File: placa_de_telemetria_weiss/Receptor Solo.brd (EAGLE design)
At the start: 61.9 x 84.3 mm, 6 parts

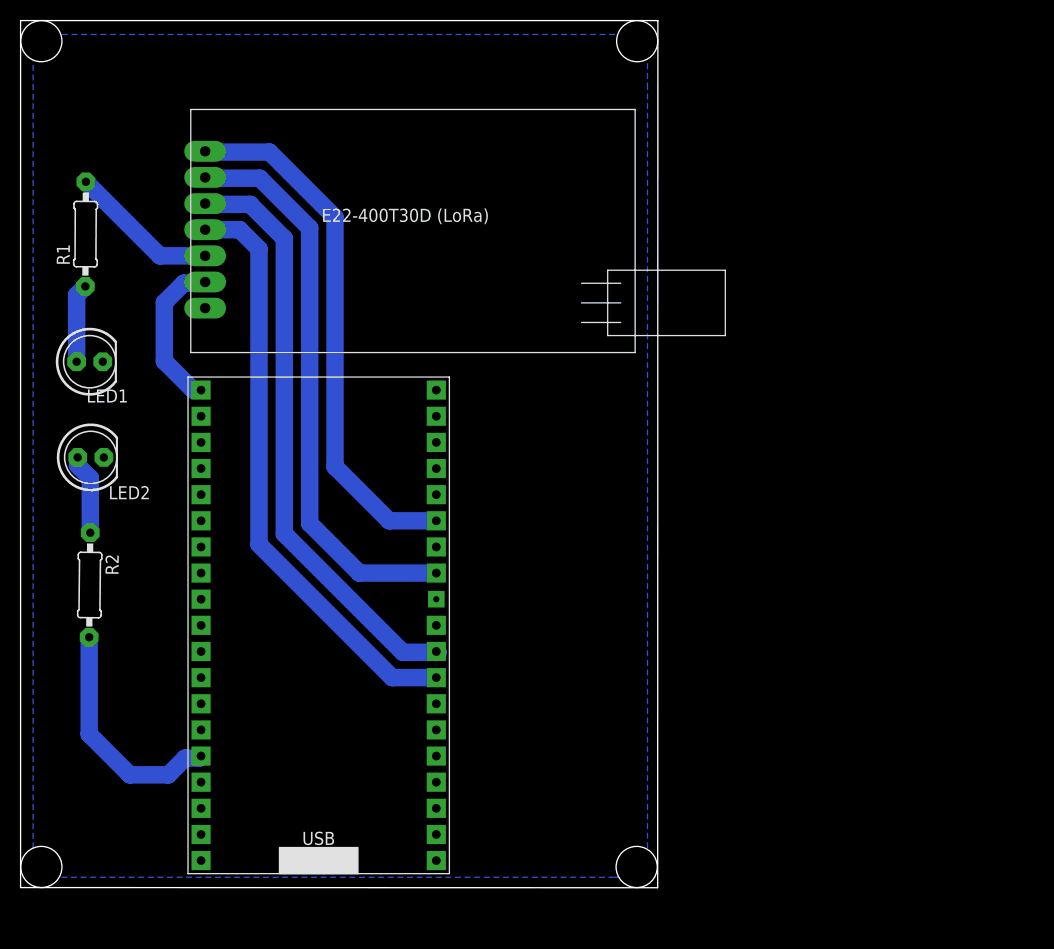
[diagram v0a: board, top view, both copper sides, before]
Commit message: fix(pcb): substitui ESP32 incorreto e adiciona furos de fixação à placa de telemetria
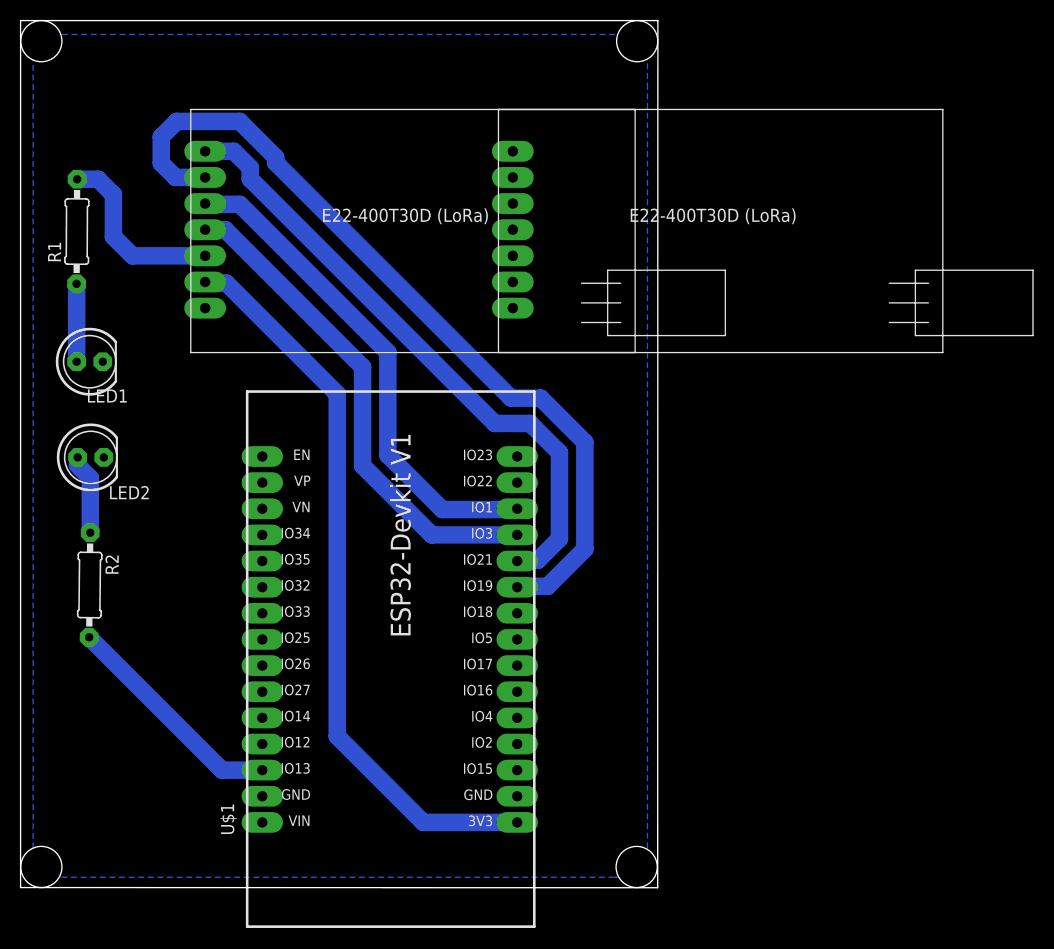
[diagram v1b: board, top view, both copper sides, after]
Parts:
- added FUROSDEAPOIOLORA: E22-400T30D, CRD:E22-400T30D_FOOTPRINT
- U$1: value ESP32 -> ESP32DEVKITV1; device esp32:ESP32 -> ESP32-DEVKITV1:ESP32-DEVKITV1
- moved U$1 33.4 mm to (49.0, 26.6), turned to 90 degrees
- moved R1 0.89 mm to (19.7, 61.1)
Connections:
- net N$6 renamed AUX
- removed net N$1: U$1.GPIO21, U$2.M0
- removed net N$2: U$1.GPIO19, U$2.M1
- removed net N$3: U$1.GPIO17, U$2.RXD
- removed net N$4: U$1.GPIO16, U$2.TXD
- removed net N$5: R2.2, U$1.GPIO13
- removed net VCC: U$1.3.3V, U$2.VCC
- new net 3.3V: U$1.1, U$2.VCC
- new net GPIO13: R2.2, U$1.28
- new net GPIO19: U$1.10, U$2.M1
- new net GPIO21: U$1.11, U$2.M0
- new net RXLORA: U$1.13, U$2.RXD
- new net TXLORA: U$1.12, U$2.TXD
- net GND: now also U$1.2, U$1.29; no longer U$1.GND1
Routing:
- net GPIO19: track 0.00 -> 80.8 mm
- net 3.3V: track 0.00 -> 71.6 mm
- net GPIO21: track 0.00 -> 60.5 mm
- net N$3: track 57.7 -> 0.00 mm
- net N$4: track 57.3 -> 0.00 mm
- net N$2: track 55.2 -> 0.00 mm
- net N$1: track 51.5 -> 0.00 mm
- net RXLORA: track 0.00 -> 48.4 mm
- net TXLORA: track 0.00 -> 48.2 mm
- net N$5: track 22.7 -> 0.00 mm
- net GPIO13: track 0.00 -> 22.2 mm
- net VCC: track 15.2 -> 0.00 mm
- net AUX: track 14.6 -> 17.9 mm
